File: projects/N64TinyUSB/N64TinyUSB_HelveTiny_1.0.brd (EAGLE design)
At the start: 20.1 x 37.3 mm, 24 parts, among them U1 ATTINY85-20PU

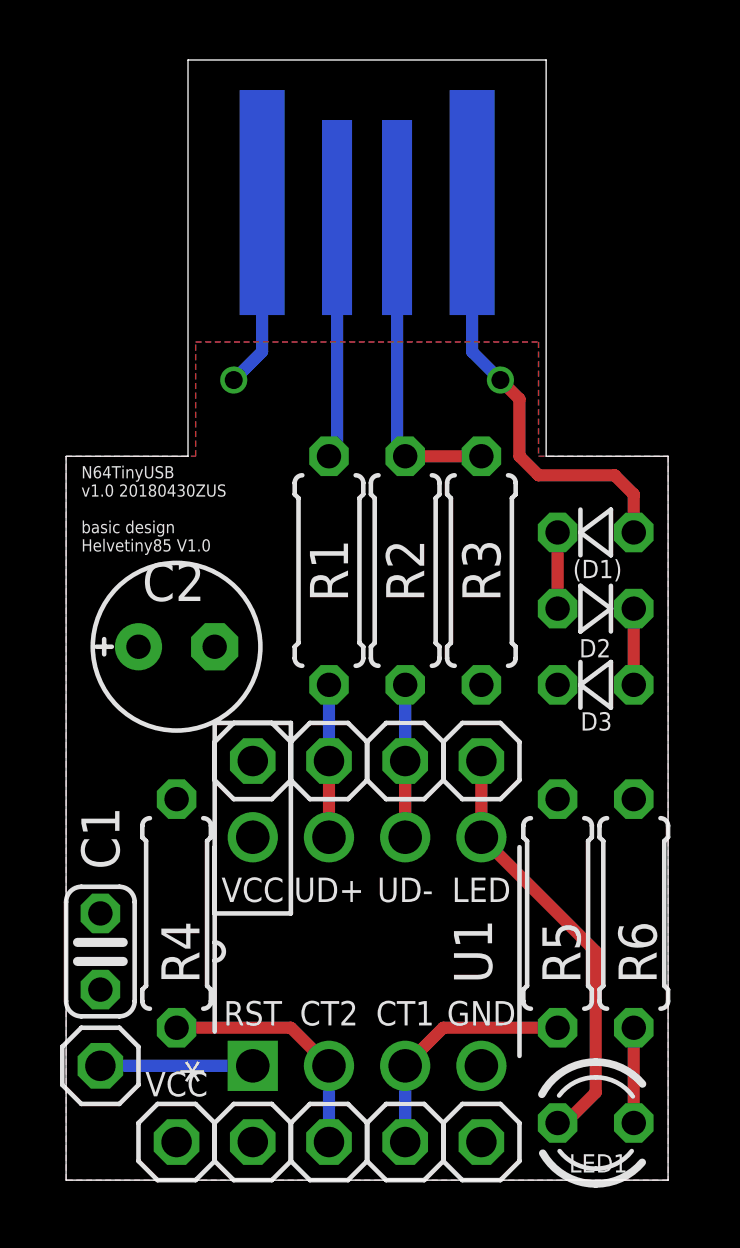
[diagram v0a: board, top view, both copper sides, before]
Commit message: improvement; N64TinyUSB v1.1              * pol-cap position              * text placement and size (2 parts, v1.1, date)              * thermals width 5              * diode type 1N4150              * run tests and aprove 1 error
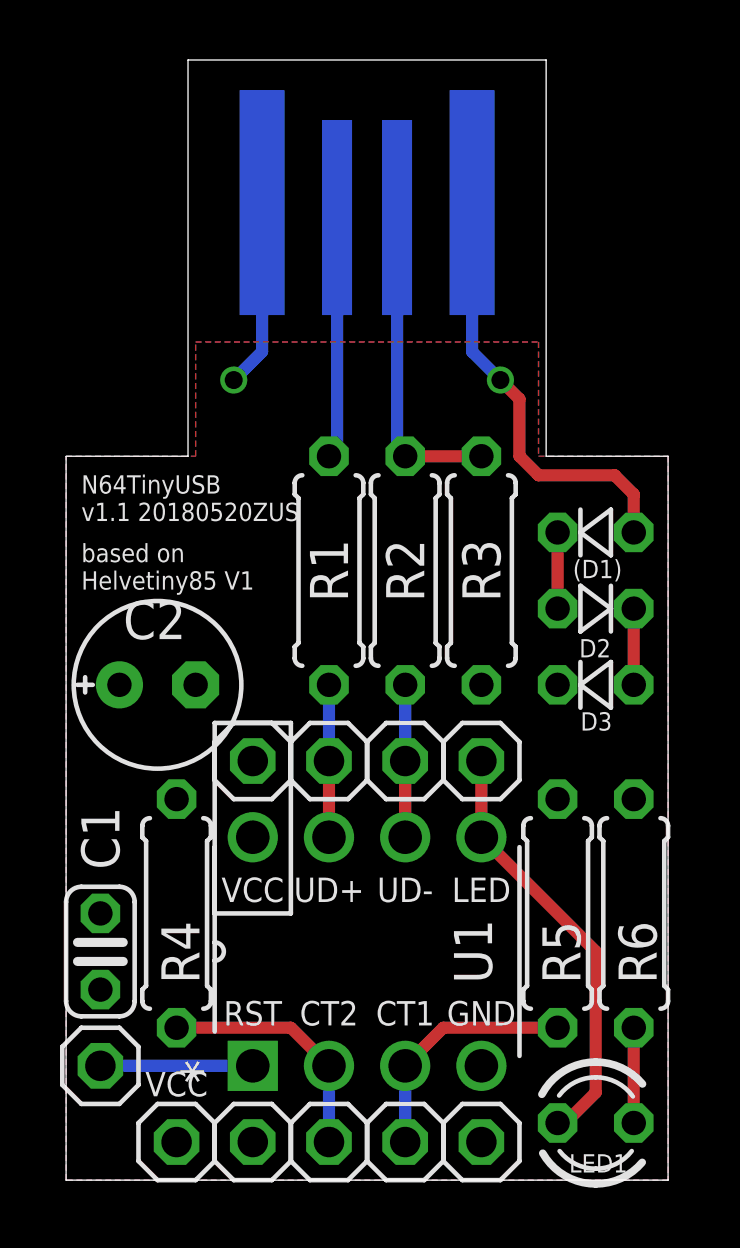
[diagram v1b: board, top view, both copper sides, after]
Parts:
- (D1), D2, D3: value 1N? -> 1N4150
- moved C2 1.42 mm to (2.54, 15.2)
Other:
- board text added: "N64TinyUSB v1.1 20180520ZUS"
- board text added: "based on Helvetiny85 V1"
- board text removed: "N64TinyUSB v1.0 20180430ZUS basic design Helvetiny85 V1.0"
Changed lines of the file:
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@@
 <wire x1="15.494" y1="36.068" x2="15.494" y2="22.86" width="0" layer="20"/>
 <wire x1="15.494" y1="22.86" x2="19.558" y2="22.86" width="0" layer="20"/>
-<text x="0" y="19.685" size="0.4064" layer="25" font="vector">N64TinyUSB
-v1.0 20180430ZUS
-basic design
-Helvetiny85 V1.0</text>
+<text x="0" y="22.225" size="0.6096" layer="25" font="vector" align="top-left">N64TinyUSB
+v1.1 20180520ZUS</text>
 <text x="5.715" y="8.001" size="0.8128" layer="25" rot="R180" align="top-center">VCC</text>
 <text x="5.715" y="4.699" size="0.8128" layer="25" rot="SR0" align="top-center">RST</text>
@@
 <dimension x1="15.494" y1="36.068" x2="15.494" y2="22.86" x3="24.13" y3="29.464" textsize="1.778" layer="51"/>
 <dimension x1="3.556" y1="36.068" x2="15.494" y2="36.068" x3="9.525" y3="40.64" textsize="1.778" layer="51"/>
+<text x="0" y="18.415" size="0.6096" layer="25" font="vector">based on
+Helvetiny85 V1</text>
 </plain>
 <attributes>
@@
 <attribute name="VALUE" x="2.6162" y="9.906" size="1.27" layer="27" ratio="10" rot="R270"/>
 </element>
-<element name="C2" library="rcl" package="E2,5-6E" value="4u7" x="3.175" y="16.51" smashed="yes">
-<attribute name="NAME" x="2.032" y="18.034" size="1.27" layer="25" ratio="10"/>
-<attribute name="VALUE" x="1.778" y="13.97" size="1.27" layer="27" ratio="10"/>
+<element name="C2" library="rcl" package="E2,5-6E" value="4u7" x="2.54" y="15.24" smashed="yes">
+<attribute name="NAME" x="1.397" y="16.764" size="1.27" layer="25" ratio="10"/>
+<attribute name="VALUE" x="1.143" y="12.7" size="1.27" layer="27" ratio="10"/>
 </element>
 <element name="LED1" library="led" package="LED3MM" value="red" x="17.145" y="0.635" smashed="yes">
@@
 <attribute name="VALUE" x="17.8562" y="9.906" size="1.27" layer="27" ratio="10" rot="R270"/>
 </element>
-<element name="(D1)" library="diode" package="D-2.5" value="1N?" x="17.145" y="20.32" smashed="yes">
+<element name="(D1)" library="diode" package="D-2.5" value="1N4150" x="17.145" y="20.32" smashed="yes">
 <attribute name="NAME" x="16.383" y="18.796" size="0.6096" layer="25" ratio="10"/>
 <attribute name="VALUE" x="15.494" y="17.907" size="1.27" layer="27" ratio="10" display="off"/>
 </element>
-<element name="D2" library="diode" package="D-2.5" value="1N?" x="17.145" y="17.78" smashed="yes" rot="R180">
+<element name="D2" library="diode" package="D-2.5" value="1N4150" x="17.145" y="17.78" smashed="yes" rot="R180">
 <attribute name="NAME" x="17.653" y="16.764" size="0.6096" layer="25" ratio="10" rot="R180"/>
 <attribute name="VALUE" x="18.796" y="20.193" size="1.27" layer="27" ratio="10" rot="R180" display="off"/>
 </element>
-<element name="D3" library="diode" package="D-2.5" value="1N?" x="17.145" y="15.24" smashed="yes">
+<element name="D3" library="diode" package="D-2.5" value="1N4150" x="17.145" y="15.24" smashed="yes">
 <attribute name="NAME" x="16.637" y="13.716" size="0.6096" layer="25" ratio="10"/>
 <attribute name="VALUE" x="15.494" y="12.827" size="1.27" layer="27" ratio="10" display="off"/>
@@
 <contactref element="C2" pad="+"/>
 <contactref element="D3" pad="C"/>
-<polygon width="0.254" layer="1">
+<polygon width="0.127" layer="1">
 <vertex x="3.81" y="26.67"/>
 <vertex x="15.24" y="26.67"/>
@@
 <contactref element="JP1" pad="GND"/>
 <contactref element="C1" pad="2"/>
-<polygon width="0.254" layer="16">
+<polygon width="0.127" layer="16">
 <vertex x="3.81" y="26.67"/>
 <vertex x="15.24" y="26.67"/>
